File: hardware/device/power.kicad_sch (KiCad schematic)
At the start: 38 parts, among them IC3 SP3401-02UTG, J1 POT_CONN, J2 USB, U20 TPS62A02DRL, U21 TPS560200, U22 MAX17261xxTD, U23 BQ21040DBV, U26 FUSB303BTMX, U27 FUSB302B01MPX, U31 FUSB302B01MPX

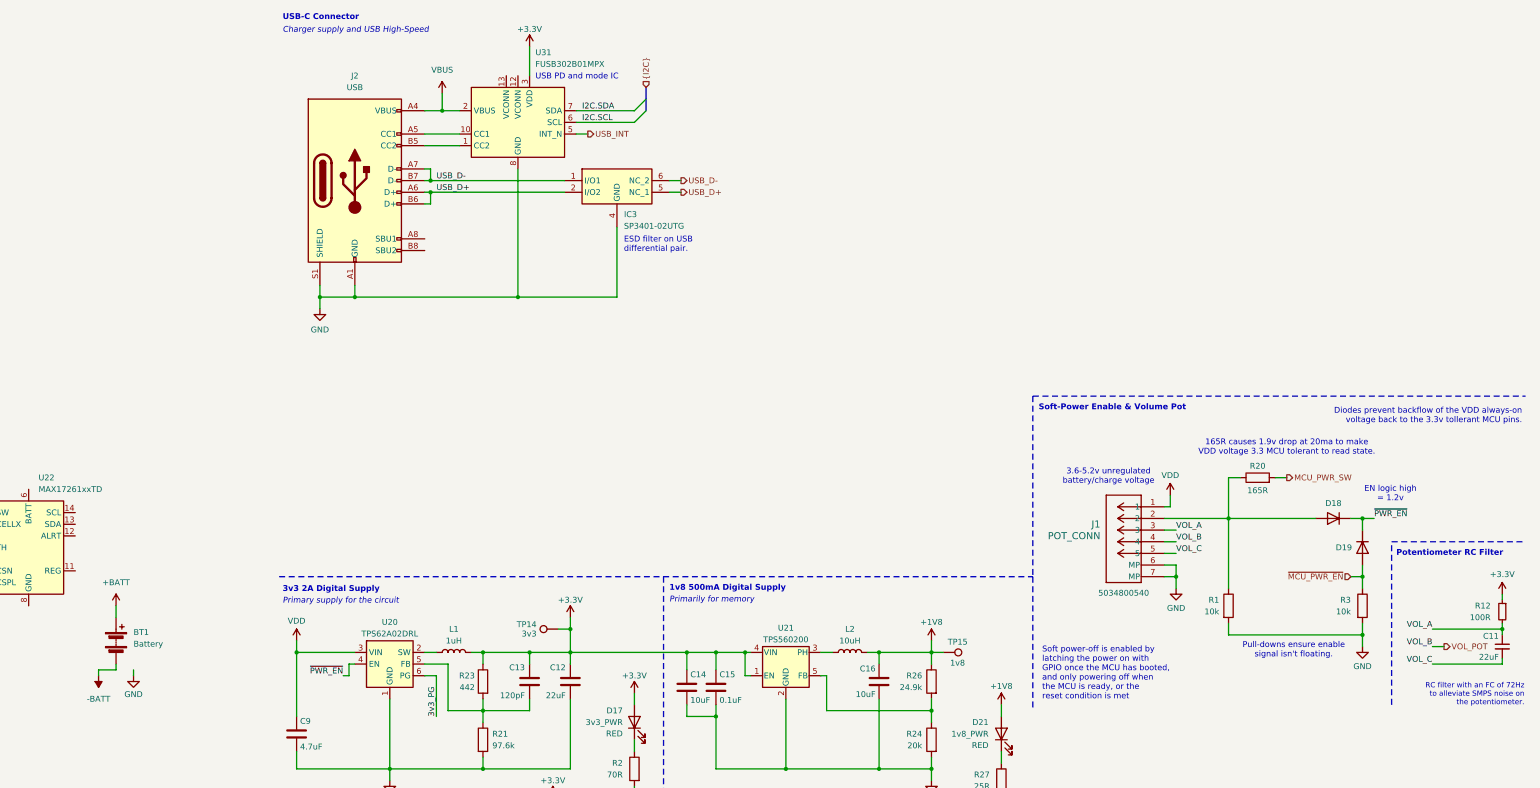
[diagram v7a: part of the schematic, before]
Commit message: feat: start adding battery fuel gauge
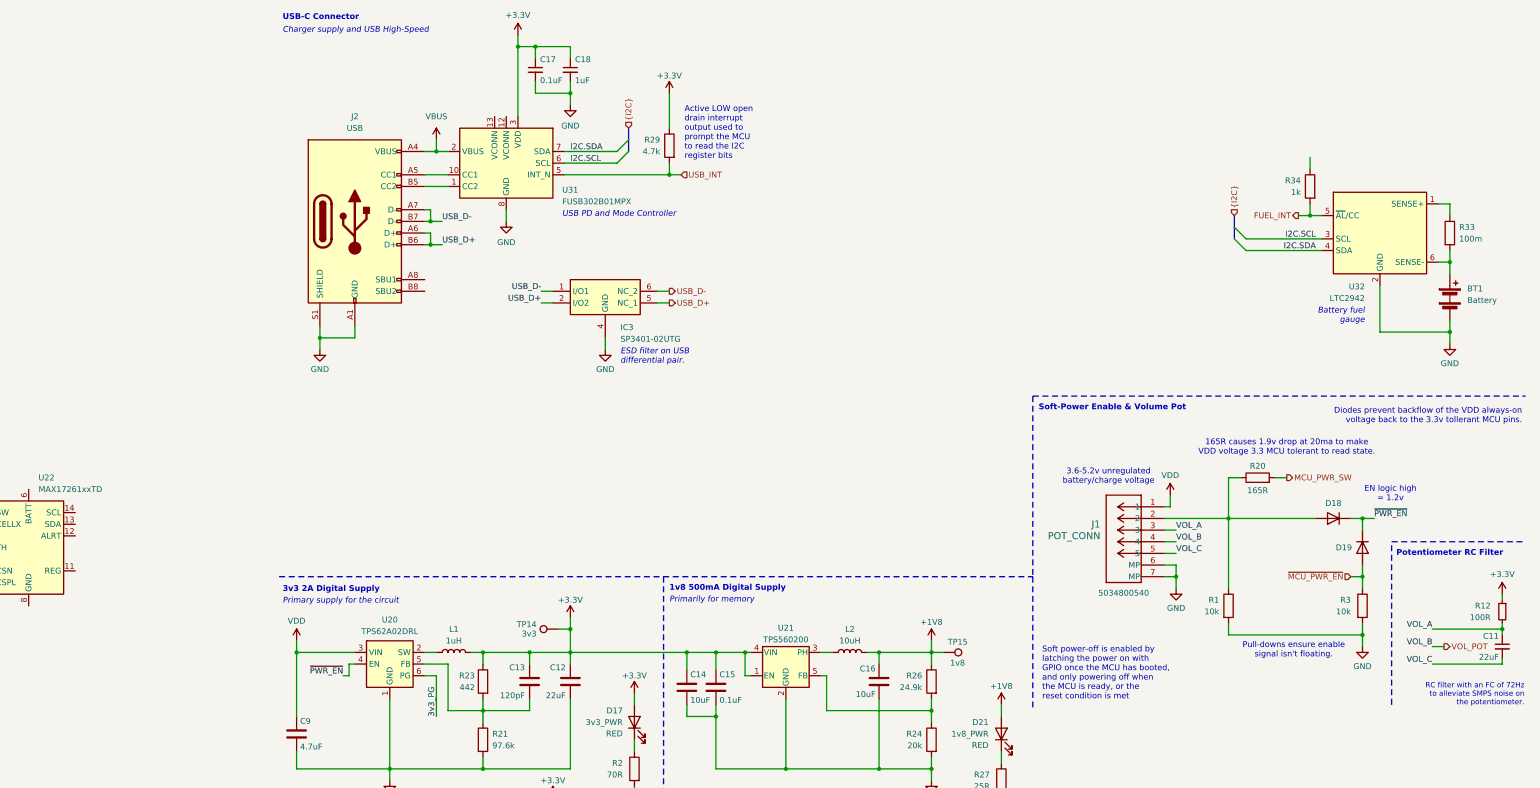
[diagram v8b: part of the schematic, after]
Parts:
- added C17: 0.1uF, symbol Device:C_Small
- added C18: 1uF, symbol Device:C_Small
- added R29: 4.7k, symbol Device:R
- added R33: 100m, symbol Device:R
- added R34: 1k, symbol Device:R
- added U32: LTC2942, Package_DFN_QFN:DFN-6-1EP_3x2mm_P0.5mm_EP1.65x1.35mm, symbol Battery_Management:LTC2942
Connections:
- net -BATT is gone; now on net GND: BT1.2 (-)
- net +3.3V: now also C17.1, C18.1, R29.1
- net GND: now also C17.2, C18.2, U32.2 (GND)
- net I2C.SCL: now also U32.3 (SCL)
- net I2C.SDA: now also U32.4 (SDA)
- net USB_INT: now also R29.2
- net +BATT: no longer names the net of BT1.1 (+)
- net +BATT: now also R33.2, U32.6 (SENSE-)
- new net: R33.1, U32.1 (SENSE+)
- new net FUEL_INT: R34.2, U32.5 (~{AL}/CC)
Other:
- note added: "Active LOW open drain interrupt output used to prompt the MCU to read the I2C register bits"
- note added: "Battery fuel gauge"
- note added: "USB PD and Mode Controller"
- note removed: "USB PD and mode IC"
- moved on the sheet: BT1, IC3, J2, U31
